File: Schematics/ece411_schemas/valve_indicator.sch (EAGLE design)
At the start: 73 parts, among them J1 1.27MM-SWD-CONNECTOR, T1 2N2222, T2 2N2222, T3 2N2222, T4 2N2222, U1 DIODES_INC._AZ34063UMTR-G1DIO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, U2 DIODES_INC._AZ34063UMTR-G1DIO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, U3 STM32F042K6

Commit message: bom, layout, attribute, device
added attributes to rest of parts
made power lines thicker for dissapation
editted az34.. device to remedy errors
added test points
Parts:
- removed J1: 1.27MM-SWD-CONNECTOR, J-CNC-3220-10-0100-00-ARM-SWD-port:1.27MM-SWD-CONNECTOR
- added CM1: FTSH-105-XX-X-DV-K, J-Samtec-FTSH-105-XXX-DV-K-ARM-SWD:FTSH-105-XX-X-DV-K
- added TP10V, TP3V3, TP3V3J, TPJGND, TPNRST, TPOE, TPSCLK, TPSIO: TEST-POINT-LARGE-SQUARE, oresat-misc:TEST-POINT-LARGE-SQUARE
- C0_H, C0_L: DIS (none) -> Digi-Key; DPN (none) -> 1276-6736-1-ND; MFR (none) -> Samsung Electro-Mechanics; MPN (none) -> CL31A106MBHNNNE
- C10, C11, C12: DIS (none) -> Digi-Key; DPN (none) -> 1276-1006-1-ND; MFR (none) -> Samsung Electro-Mechanics; MPN (none) -> CL10B104KA8NNNC
- D1: value ON_SEMICONDUCTOR_1N5819GON_SEMICONDUCTOR_1N5819G_0_0 -> 1N5819G_0_0
- D2: value ON_SEMICONDUCTOR_1N5819GON_SEMICONDUCTOR_1N5819G_0_0 -> 1N5819G_0_0; MFR ON Semiconductor -> (none)
- D3: DIS (none) -> Digi-Key; DPN (none) -> SB240-E3/54GICT-ND; MFR (none) -> Vishay Semiconductor Diodes Division; MPN (none) -> SB240-E3/54
- R1_L: DPN RMCF0603FT4K70CT-ND -> 311-3.60KHRCT-ND; MFR Stackpole Electronics Inc -> Yageo; MPN RMCF0603FT4K70 -> RC0603FR-073K6L
- R2_L: DPN RNCP0603FTD2K49CT-ND -> P2.20KHCT-ND; MFR Stackpole Electronics Inc -> Panasonic Electronic Components; MPN RNCP0603FTD2K49 -> ERJ-3EKF2201V
- U1, U2: value DIODES_INC._AZ34063UMTR-G1DIODES_INC._AZ34063UMTR-G1_0_0 -> AZ34063UMTR-G1
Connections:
- removed net +12V: BUZZER.1, C3_H.1, HES1.1, HES2.1, HES3.1, HES4.1, HES5.1, HES6.1, HES7.1, HES8.1, HES9.1, L2.2, LED1.1, LED2.1, LED3.1, R1.1, R1_H.2, R2.1, R3.1, R4.1, R5.1, R6.1, R7.1, R8.1, R9.1
- removed net N$1: C0_H.1, C0_L.1, C1_H.1, C1_L.1, D3.C, POE_IN.PWR, RS_H.1, RS_L.1, U1.VCC, U2.VCC
- new net +10V: BUZZER.1, C3_H.1, HES1.1, HES2.1, HES3.1, HES4.1, HES5.1, HES6.1, HES7.1, HES8.1, HES9.1, L2.2, LED1.1, LED2.1, LED3.1, R1.1, R1_H.2, R2.1, R3.1, R4.1, R5.1, R6.1, R7.1, R8.1, R9.1, TP10V.1
- new net POE: C0_H.1, C0_L.1, C1_H.1, C1_L.1, D3.C, POE_IN.PWR, RS_H.1, RS_L.1, TPOE.1, U1.VCC, U2.VCC
- net +3V3: now also CM1.VTREF, TP3V3.1, TP3V3J.1; no longer J1.VTREF
- net GND: now also CM1.GND, CM1.GND@2, CM1.GNDDET, TPJGND.1; no longer J1.GND, J1.GND@2, J1.GNDDET
- net N$30: now also CM1.SWDIO/TMS, TPSIO.1; no longer J1.SWDIO/TMS
- net N$32: now also CM1.!RESET, TPNRST.1; no longer J1.!RESET
- net N$9: now also CM1.SWDCLK/TCK, TPSCLK.1; no longer J1.SWDCLK/TCK
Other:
- note added: "Test Point +10V"
- note added: "Test Point 3V3"
- note added: "Test Point 3V3 JTAG"
- note added: "Test Point GND JTAG"
- note added: "Test Point NRST"
- note added: "Test Point POE"
- note added: "Test Point SWDCLK"
- note added: "Test Point SWDIO"

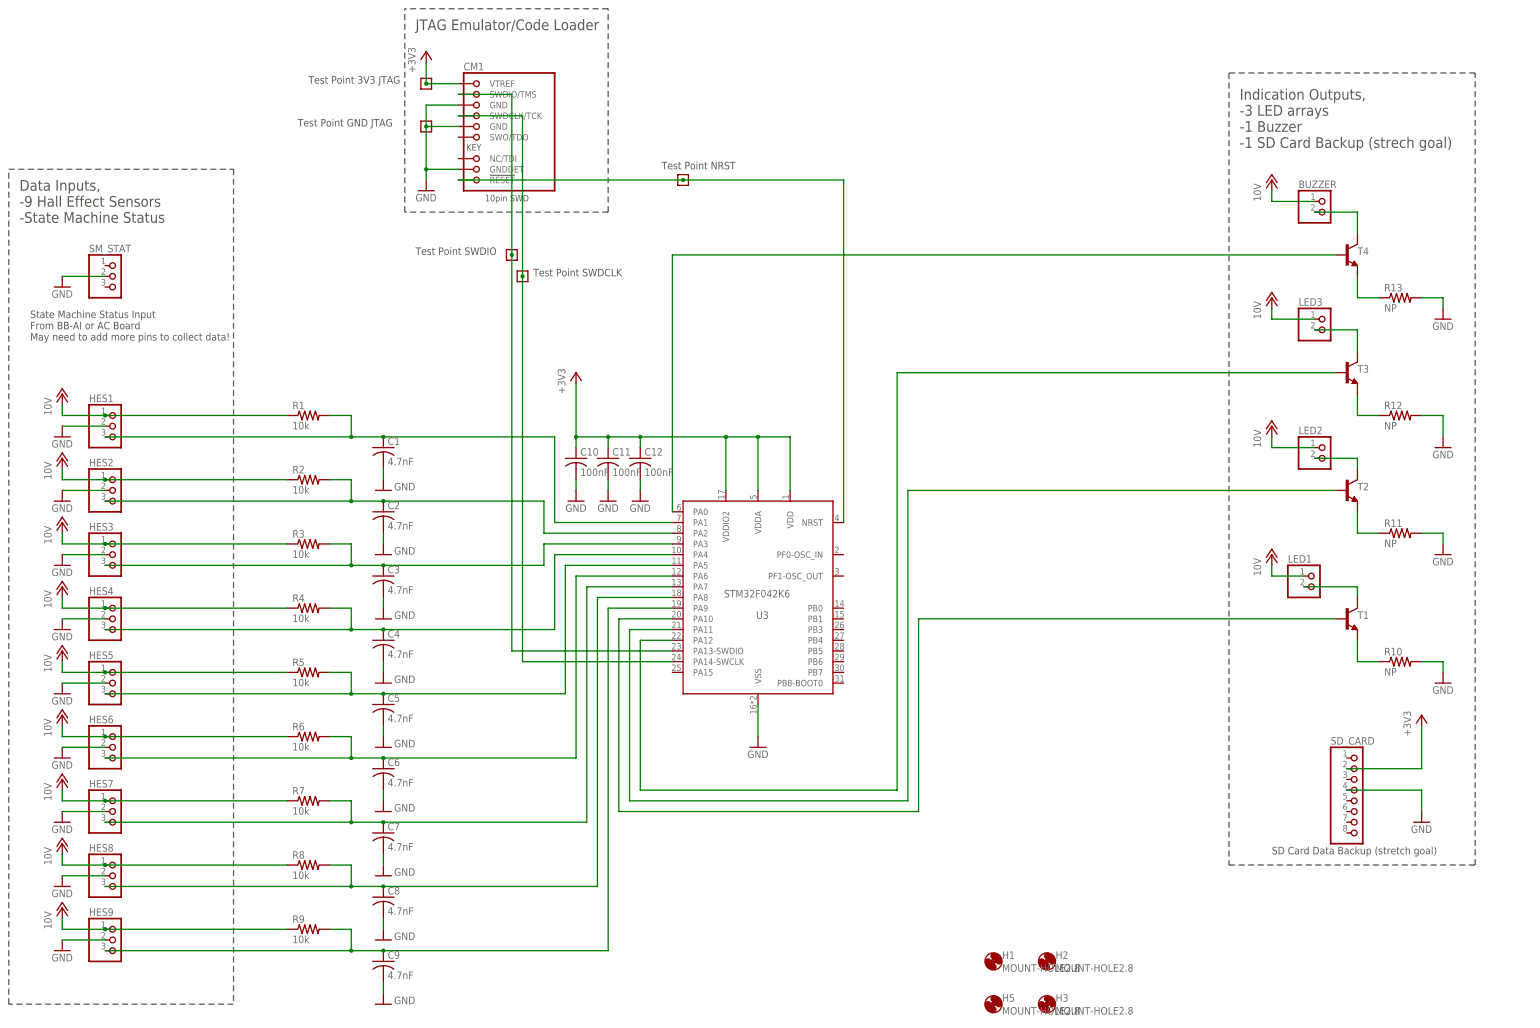
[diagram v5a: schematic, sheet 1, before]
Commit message: added state machine uart conn, labels
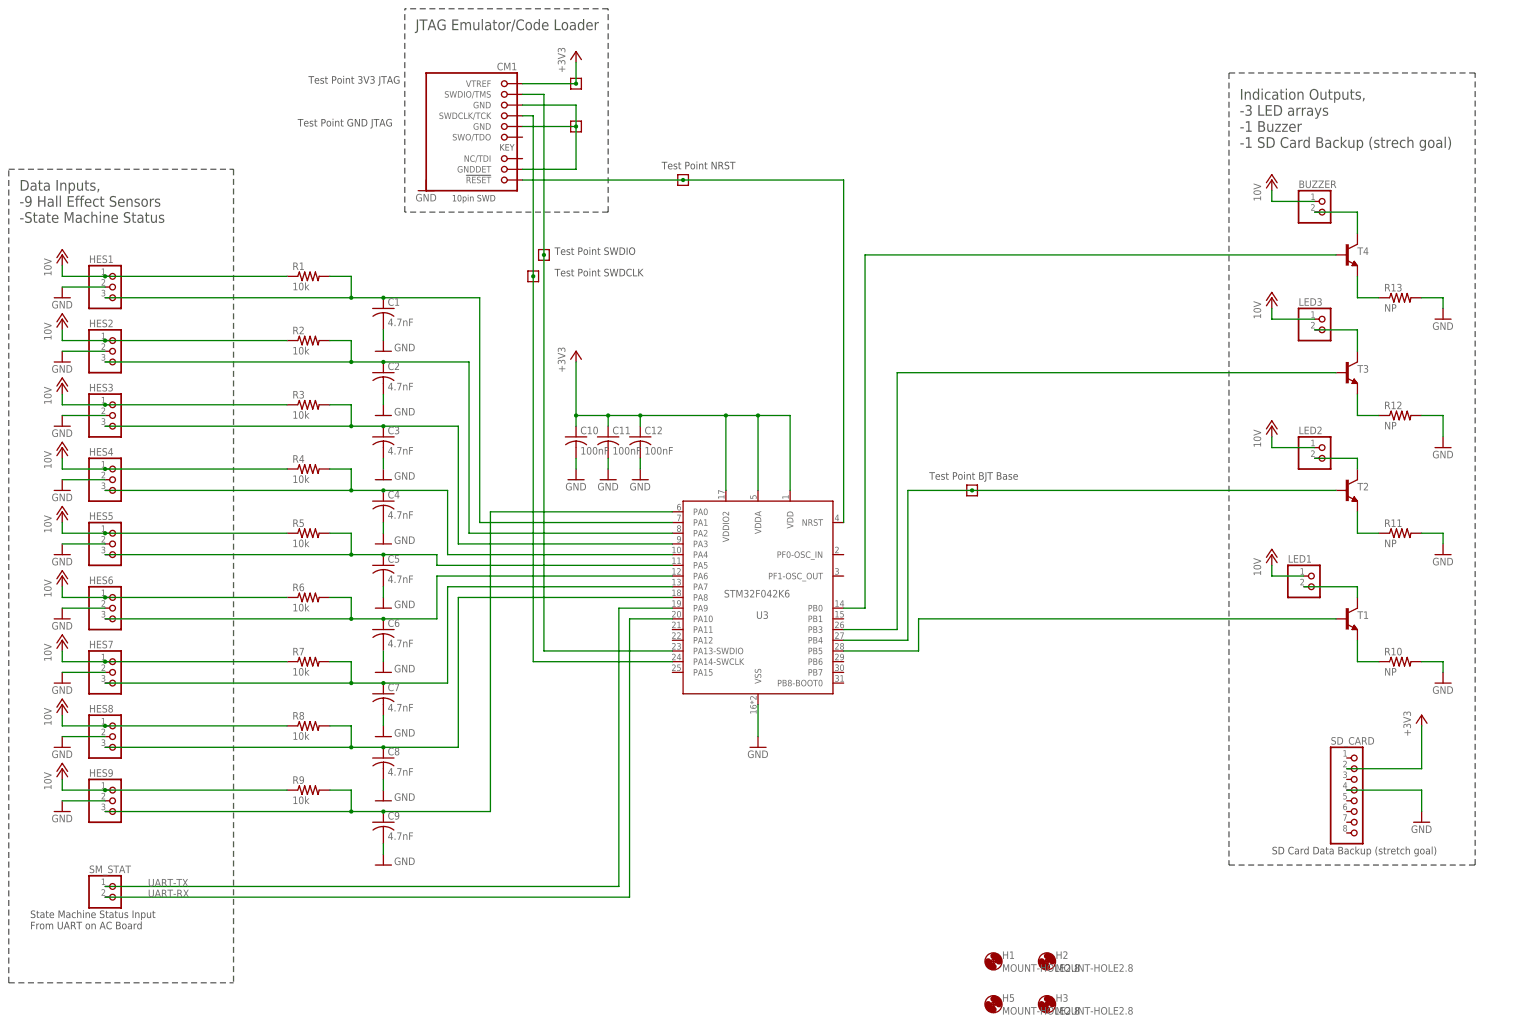
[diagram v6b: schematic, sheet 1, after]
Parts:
- added TPBASE: TEST-POINT-LARGE-SQUARE, oresat-misc:TEST-POINT-LARGE-SQUARE
- SM_STAT: device pinhead:PINHD-1X3 -> pinhead:PINHD-1X2
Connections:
- new net N$23: CM1.GND, CM1.GND@2, CM1.GNDDET, TPJGND.1
- new net UART-RX: SM_STAT.2, U3.PA10
- new net UART-TX: SM_STAT.1, U3.PA9
- net GND: no longer CM1.GND, CM1.GND@2, CM1.GNDDET, SM_STAT.2, TPJGND.1
- net N$15: now also U3.PA0; no longer U3.PA9
- net N$22: now also U3.PB5; no longer U3.PA10
- net N$24: now also U3.PB3; no longer U3.PA12
- net N$34: now also U3.PB0; no longer U3.PA0
- net N$35: now also TPBASE.1, U3.PB4; no longer U3.PA11
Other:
- note added: "State Machine Status Input From UART on AC Board"
- note added: "Test Point BJT Base"
- note removed: "State Machine Status Input From BB-AI or AC Board May need to add more pins to collect data!"
- moved on the sheet: C1, C10, C11, C12, C2, C3, C4, C5, C6, C7, C8, C9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

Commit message: updated inductor part
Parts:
- L1, L2: DIS Digi-Key -> Mouser; DPN AIUR-06-221K-ND -> 994-RFS1317-224KL; MFR Abracon LLC -> Coilcraft; MPN AIUR-06-221K -> RFS1317-224KL
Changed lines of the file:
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@@
 </pinmapping>
 </spice>
-<attribute name="DIS" value="Digi-Key"/>
-<attribute name="DPN" value="AIUR-06-221K-ND"/>
-<attribute name="MFR" value="Abracon LLC"/>
-<attribute name="MPN" value="AIUR-06-221K"/>
+<attribute name="DIS" value="Mouser"/>
+<attribute name="DPN" value="994-RFS1317-224KL"/>
+<attribute name="MFR" value="Coilcraft"/>
+<attribute name="MPN" value="RFS1317-224KL"/>
 </part>
 <part name="SM_STAT" library="pinhead" library_urn="urn:adsk.eagle:library:325" deviceset="PINHD-1X2" device="" package3d_urn="urn:adsk.eagle:package:22435/2" value="SM_STAT"/>
@@
 </pinmapping>
 </spice>
-<attribute name="DIS" value="Digi-Key"/>
-<attribute name="DPN" value="AIUR-06-221K-ND"/>
-<attribute name="MFR" value="Abracon LLC"/>
-<attribute name="MPN" value="AIUR-06-221K"/>
+<attribute name="DIS" value="Mouser"/>
+<attribute name="DPN" value="994-RFS1317-224KL"/>
+<attribute name="MFR" value="Coilcraft"/>
+<attribute name="MPN" value="RFS1317-224KL"/>
 </part>
 <part name="GND25" library="supply1" library_urn="urn:adsk.eagle:library:371" deviceset="GND" device=""/>

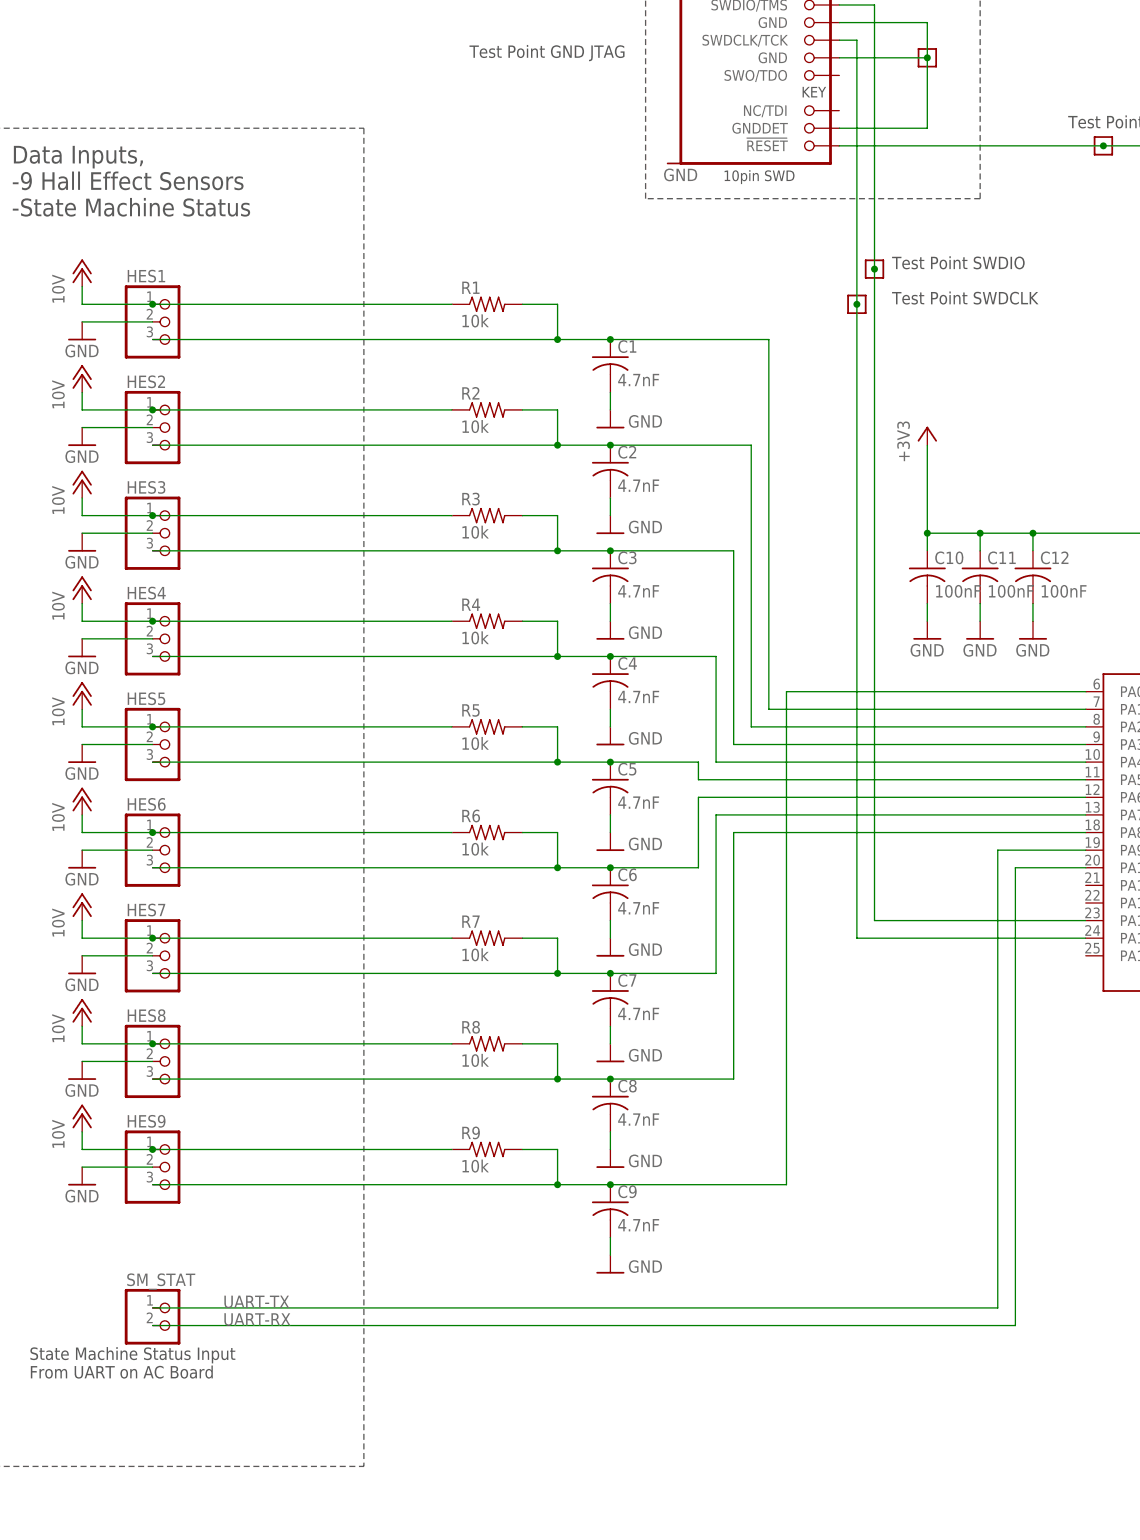
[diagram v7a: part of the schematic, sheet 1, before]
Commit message: updated board given feedback
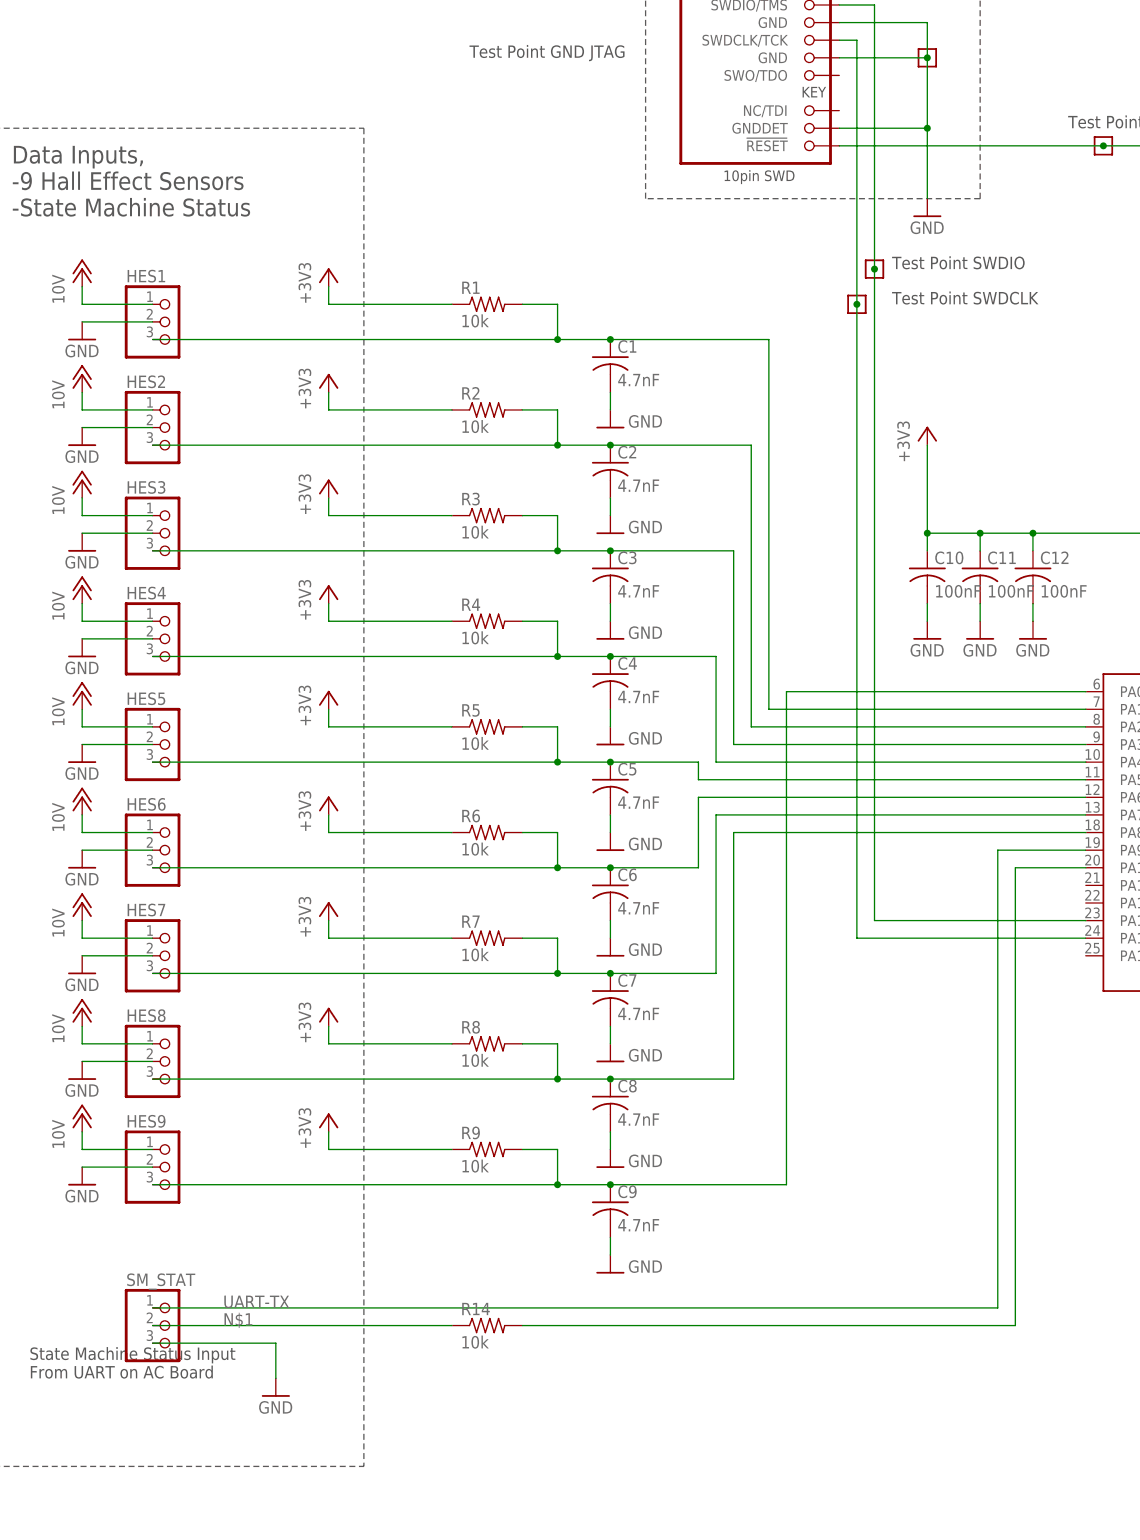
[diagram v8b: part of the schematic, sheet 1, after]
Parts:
- added R14: 10k, rcl:R-US_R0603
- SM_STAT: device pinhead:PINHD-1X2 -> pinhead:PINHD-1X3
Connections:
- removed net N$23: CM1.GND, CM1.GND@2, CM1.GNDDET, TPJGND.1
- new net N$1: R14.1, SM_STAT.2
- net +10V: no longer R1.1, R2.1, R3.1, R4.1, R5.1, R6.1, R7.1, R8.1, R9.1
- net +3V3: now also R1.1, R2.1, R3.1, R4.1, R5.1, R6.1, R7.1, R8.1, R9.1
- net GND: now also CM1.GND, CM1.GND@2, CM1.GNDDET, SM_STAT.3, TPJGND.1
- net UART-RX: now also R14.2; no longer SM_STAT.2
